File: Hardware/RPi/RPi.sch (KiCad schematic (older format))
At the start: 19 parts, among them U1 Dual_buffer_NC7WZ16

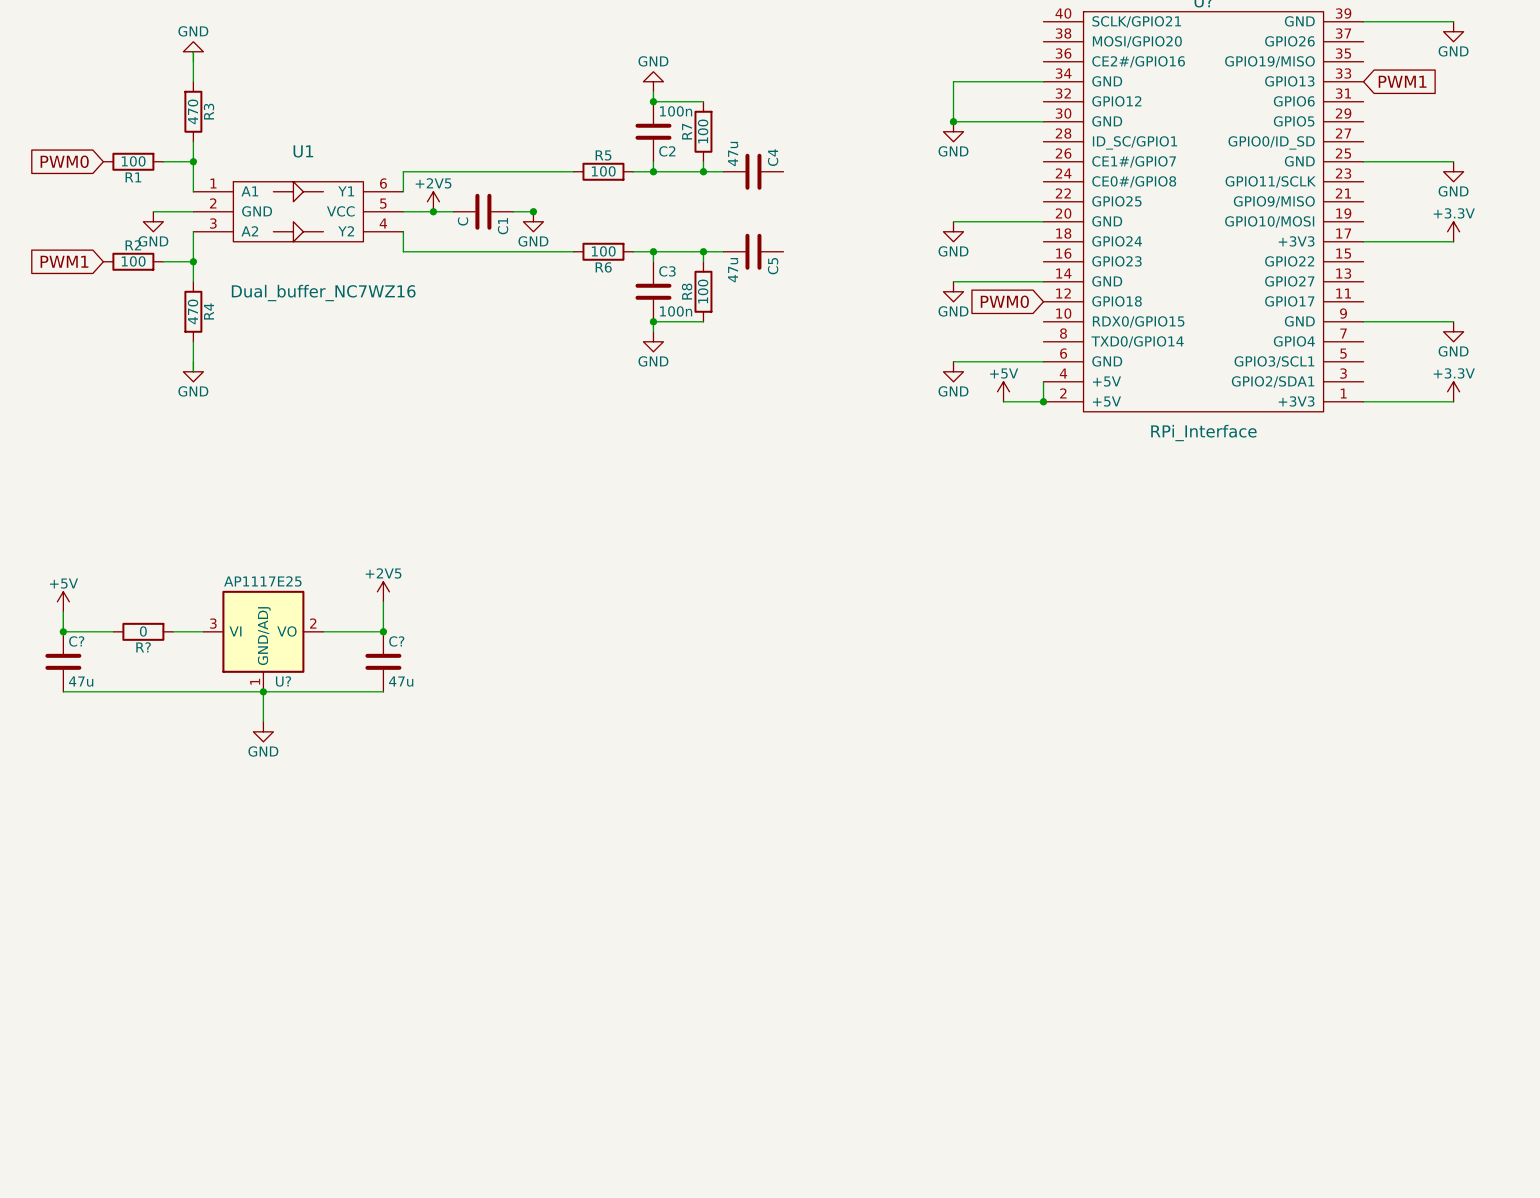
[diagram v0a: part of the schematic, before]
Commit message: Added USB hub
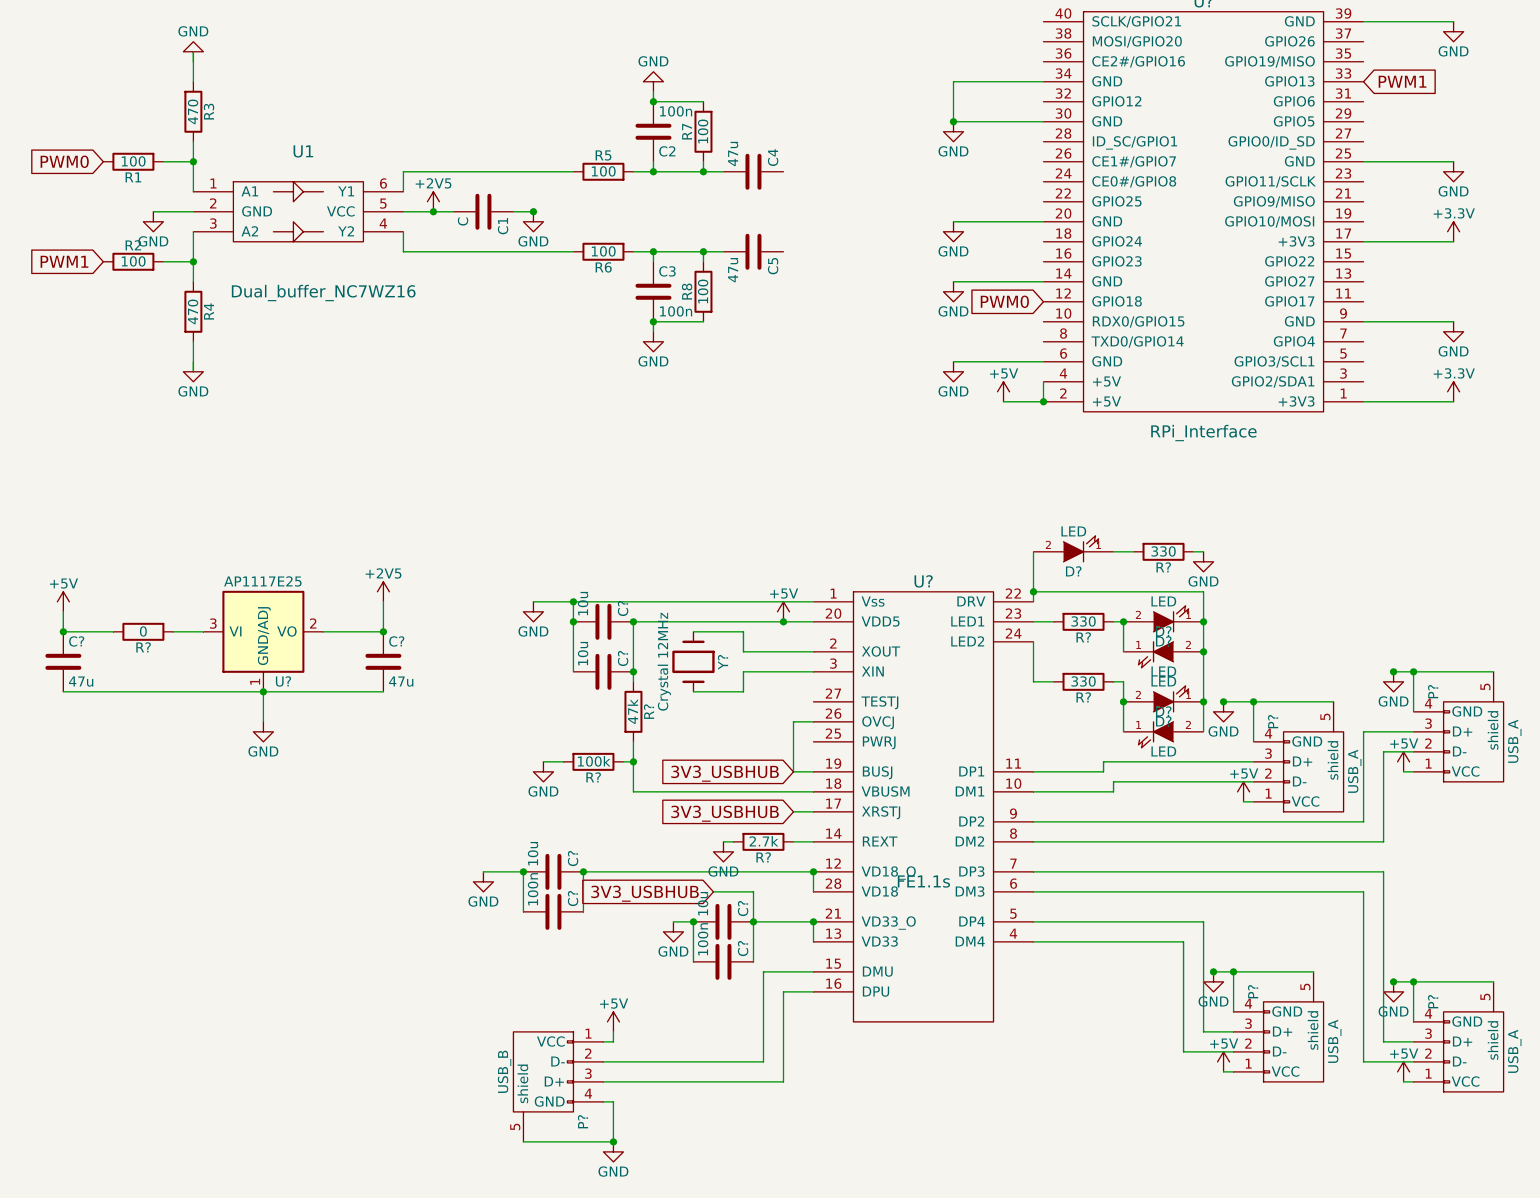
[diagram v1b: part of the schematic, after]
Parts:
- added C? (x4): 10u, symbol C
- added C? (x2): 100n, symbol C
- added D? (x5): LED, symbol LED
- added P?: USB_B, symbol USB_B
- added P? (x4): USB_A, symbol USB_A
- added R?: 47k, symbol R
- added R?: 100k, symbol R
- added R?: 2.7k, symbol R
- added R? (x3): 330, symbol R
- added U?: FE1.1s, symbol FE1.1s
- added Y?: Crystal 12MHz, symbol Crystal
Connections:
- net labels added: 3V3_USBHUB
- wire segments 43 -> 156

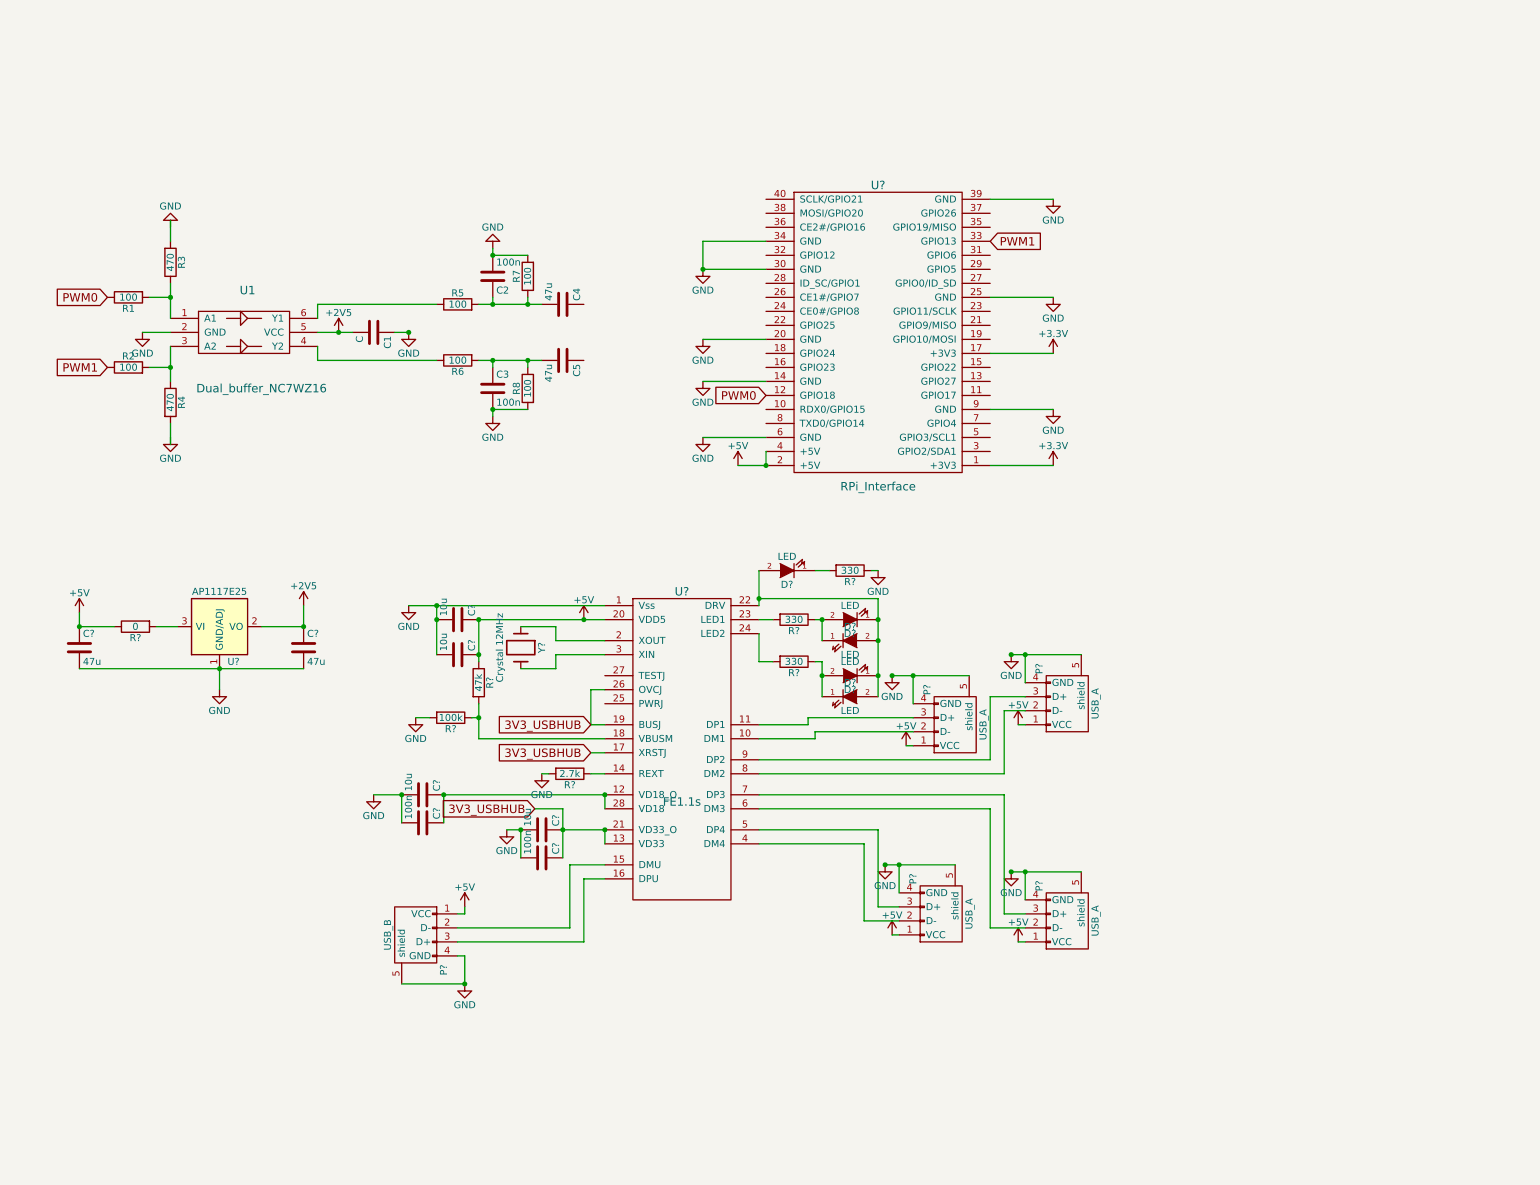
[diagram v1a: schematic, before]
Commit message: Added Teensy LC, Wake up light WS2812
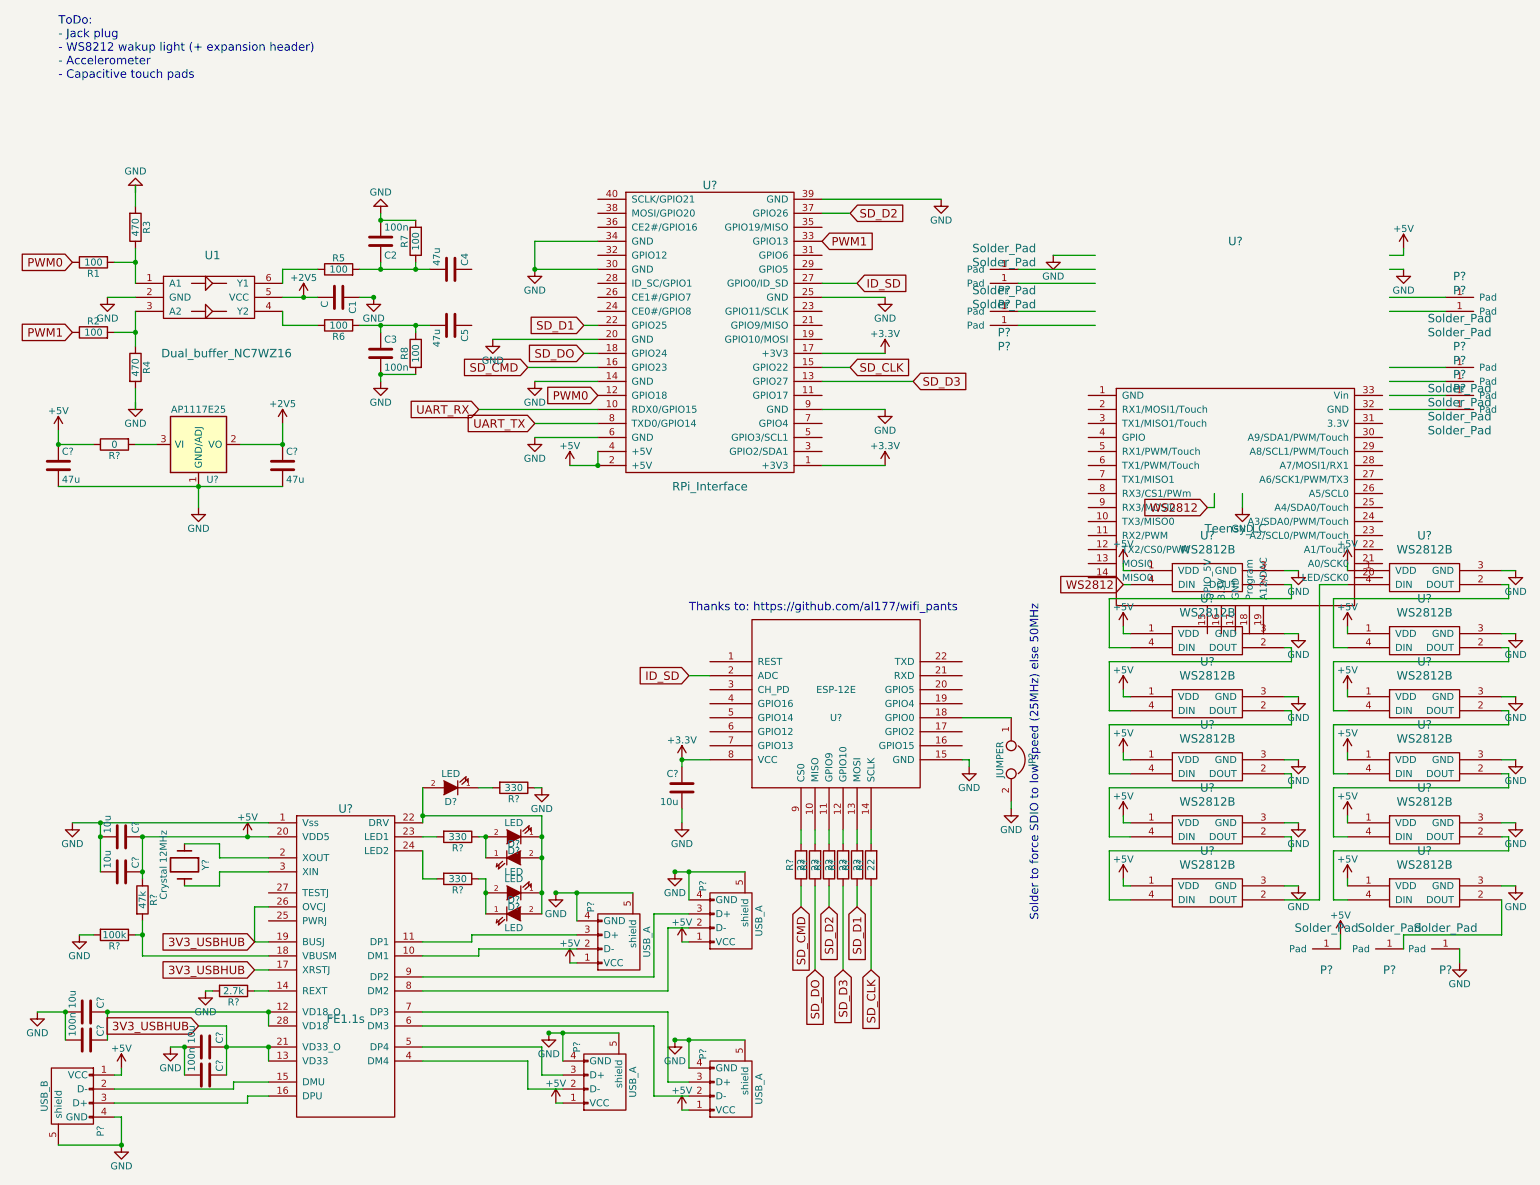
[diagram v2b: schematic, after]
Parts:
- added C?: 10u, symbol C
- added JP?: JUMPER, symbol JUMPER
- added P? (x13): Solder_Pad, symbol Solder_Pad
- added R? (x6): 22, symbol R
- added U?: ESP-12E, symbol ESP-12E
- added U?: Teensy_LC, symbol Teensy_LC
- added U? (x12): WS2812B, symbol WS2812B
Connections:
- net labels added: ID_SD, SD_CLK, SD_CMD, SD_D1, SD_D2, SD_D3, SD_DO, UART_RX, UART_TX, WS2812
- wire segments 156 -> 274
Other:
- note added: "Solder to force SDIO to low speed (25MHz) else 50MHz"
- note added: "Thanks to: https://github.com/al177/wifi_pants"
- note added: "ToDo:\n- Jack plug\n- WS8212 wakup light (+ expansion header)\n- Accelerometer\n- Capacitive touch pads"
- moved on the sheet: C1, C2, C3, C4, C5, C?, D?, P?, R1, R2, R3, R4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

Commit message: Schematic RPi
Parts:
- added C10, C14: 100n, symbol C
- added C17: 2.2n, symbol C
- added C9: 10n, symbol C
- added JP1, JP2, JP4, JP5: JUMPER, symbol JUMPER
- added P?: CONN_01X06, symbol CONN_01X06
- added R16, R17: 10k, symbol R
- added U4: MPU_9150, symbol MPU_9150
- gave numbers to parts that had none: 64
- renumbered C1 to C11, C2 to C12, C3 to C13, C4 to C15, C5 to C16, R6 to R10, R7 to R11, R8 to R12, R3 to R6, R4 to R7, R5 to R9, U1 to U2
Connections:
- net labels added: SCL, SDA
- wire segments 274 -> 311
- no-connect marks 0 -> 35
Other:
- note added: "Thanks! https://github.com/imciner2/KiCad-Libraries"
- moved on the sheet: C1, C11, C12, C13, C15, C16, C18, C2, C3, C4, C5, C6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
